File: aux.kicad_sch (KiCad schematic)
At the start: 37 parts, among them J7 USB_C_Receptacle_USB2.0_16P, J801 Conn_01x01_Pin, J802 Conn_01x01_Pin, J803 Conn_01x01_Pin, J804 Conn_01x01_Pin, J805 Conn_01x01_Pin, J806 Conn_01x01_Pin, J85 Conn_01x02_Pin, J86 Conn_01x02_Pin, Q81 AO3401A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

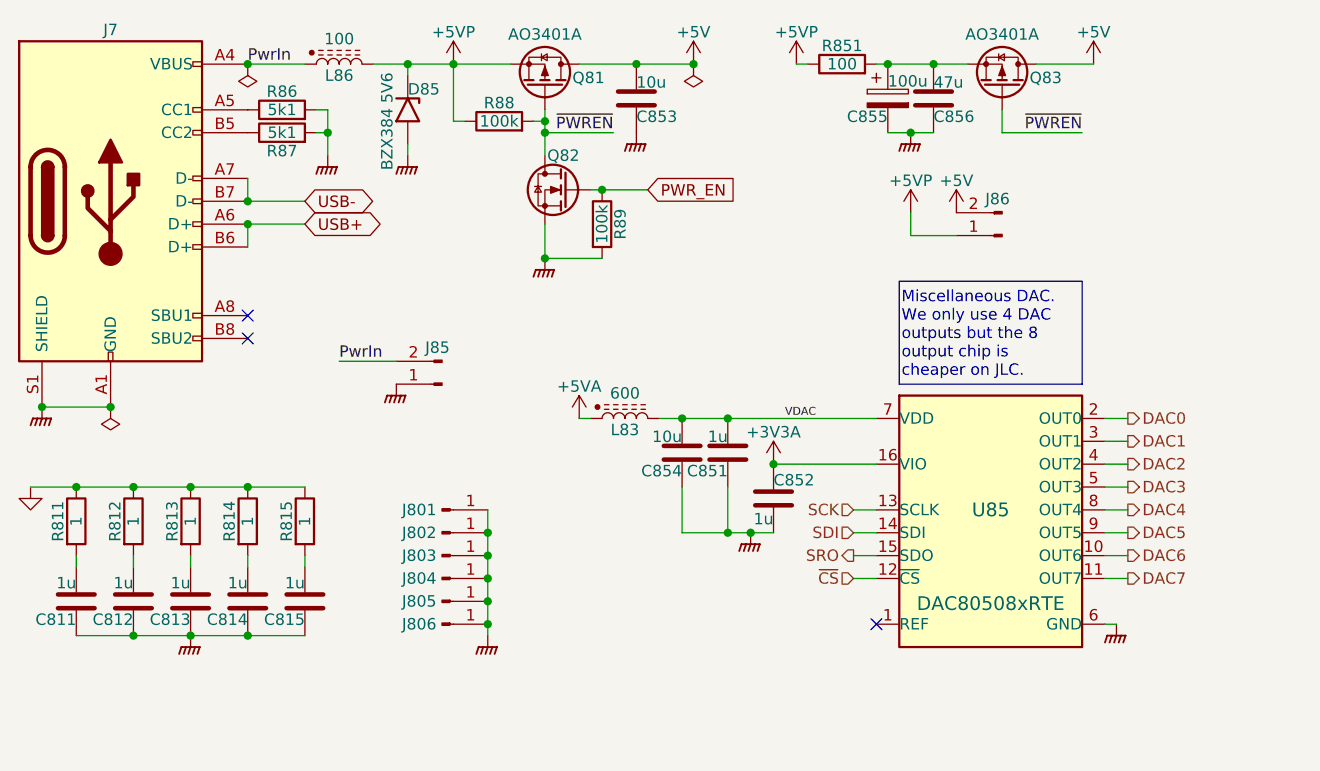
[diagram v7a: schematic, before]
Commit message: Add solder practice.  Final touchups.
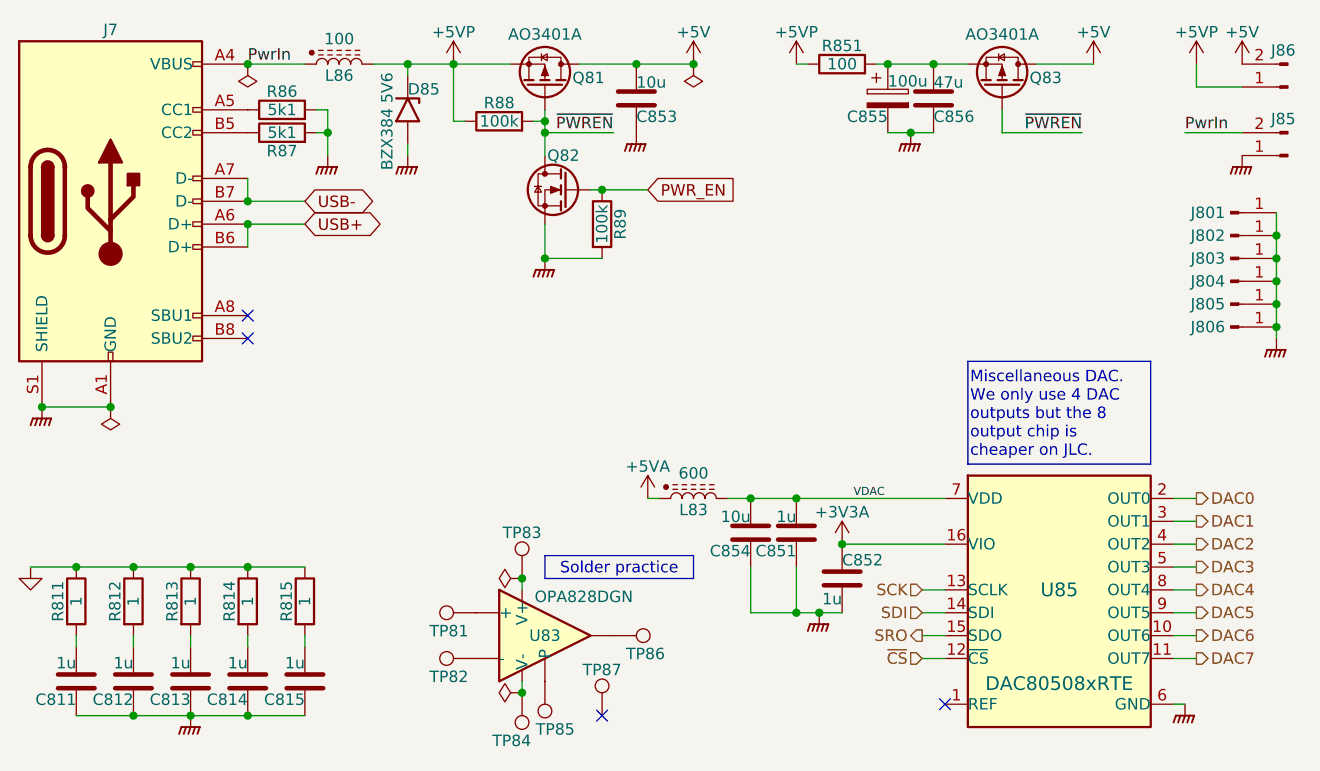
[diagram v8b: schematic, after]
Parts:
- added TP81, TP82, TP83, TP84, TP85, TP86, TP87: TestPoint, Parts:TestPoint, symbol Connector:TestPoint
- added U83: OPA828DGN, Parts:OPA828DGN_guard, symbol Parts:OPA828DGN
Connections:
- new net: TP85.1, U83.9 (P)
- new net: TP84.1, U83.4 (V-)
- new net: TP82.1, U83.2 (-)
- new net: TP81.1, U83.3 (+)
- new net: TP86.1, U83.6
- new net: TP83.1, U83.7 (V+)
- no-connect marks 3 -> 4
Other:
- moved on the sheet: C811, C812, C813, C814, C815, C851, C852, C854, J801, J802, J803, J804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
